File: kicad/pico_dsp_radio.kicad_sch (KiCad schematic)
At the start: 26 parts, among them J1 Conn_01x02, J2 MJ-8435, J3 Conn_01x12, Q1 IRLML6402, SW1 SW_SPDT, U1 Pico, U2 MCP73831-2-OT, U3 KT0913, Y1 32.768K12.5PI/4115E

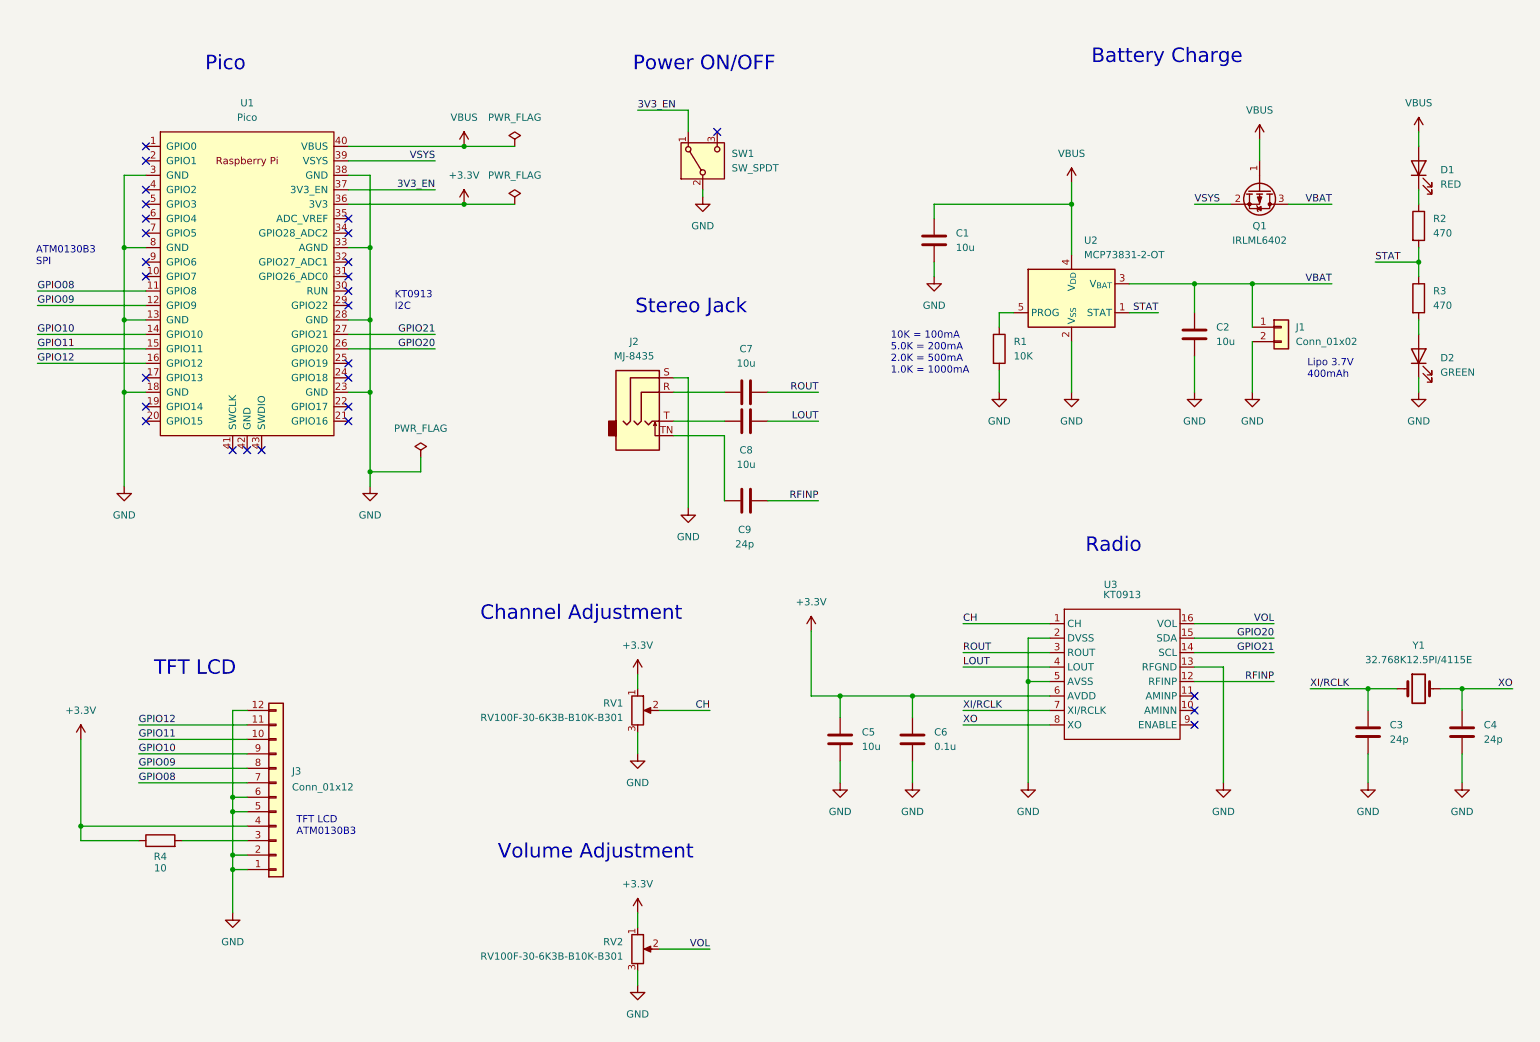
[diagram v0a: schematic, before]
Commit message: feat: Change switch to a slide switch
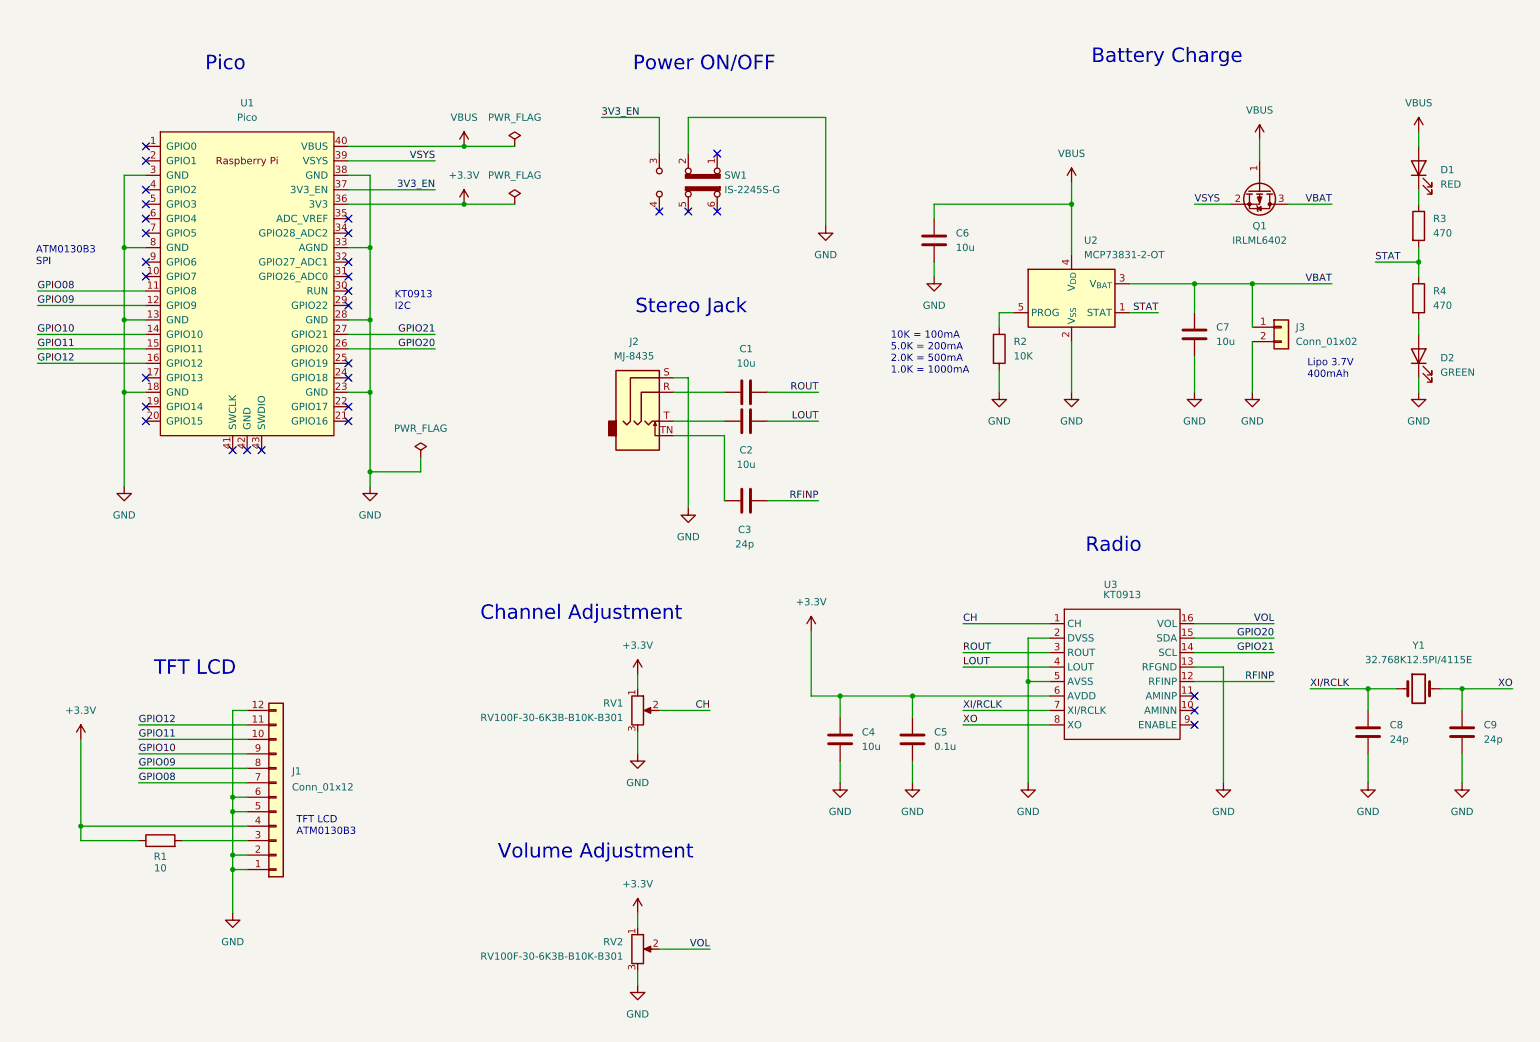
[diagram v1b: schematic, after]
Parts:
- removed SW1: SW_SPDT, symbol Switch:SW_SPDT
- added SW1: IS-2245S-G, symbol Switch:SW_Slide_DPDT
- renumbered C7 to C1, C8 to C2, C9 to C3, C5 to C4, C6 to C5, C1 to C6, C2 to C7, C3 to C8, C4 to C9, J3 to J1, J1 to J3, R4 to R1, R1 to R2, R2 to R3, R3 to R4
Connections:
- net 3V3_EN: now also SW1.3 (C)
- net GND: now also SW1.2 (B)
- no-connect marks 28 -> 31

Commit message: feat: Added a switch for toggling between the speaker and earphones
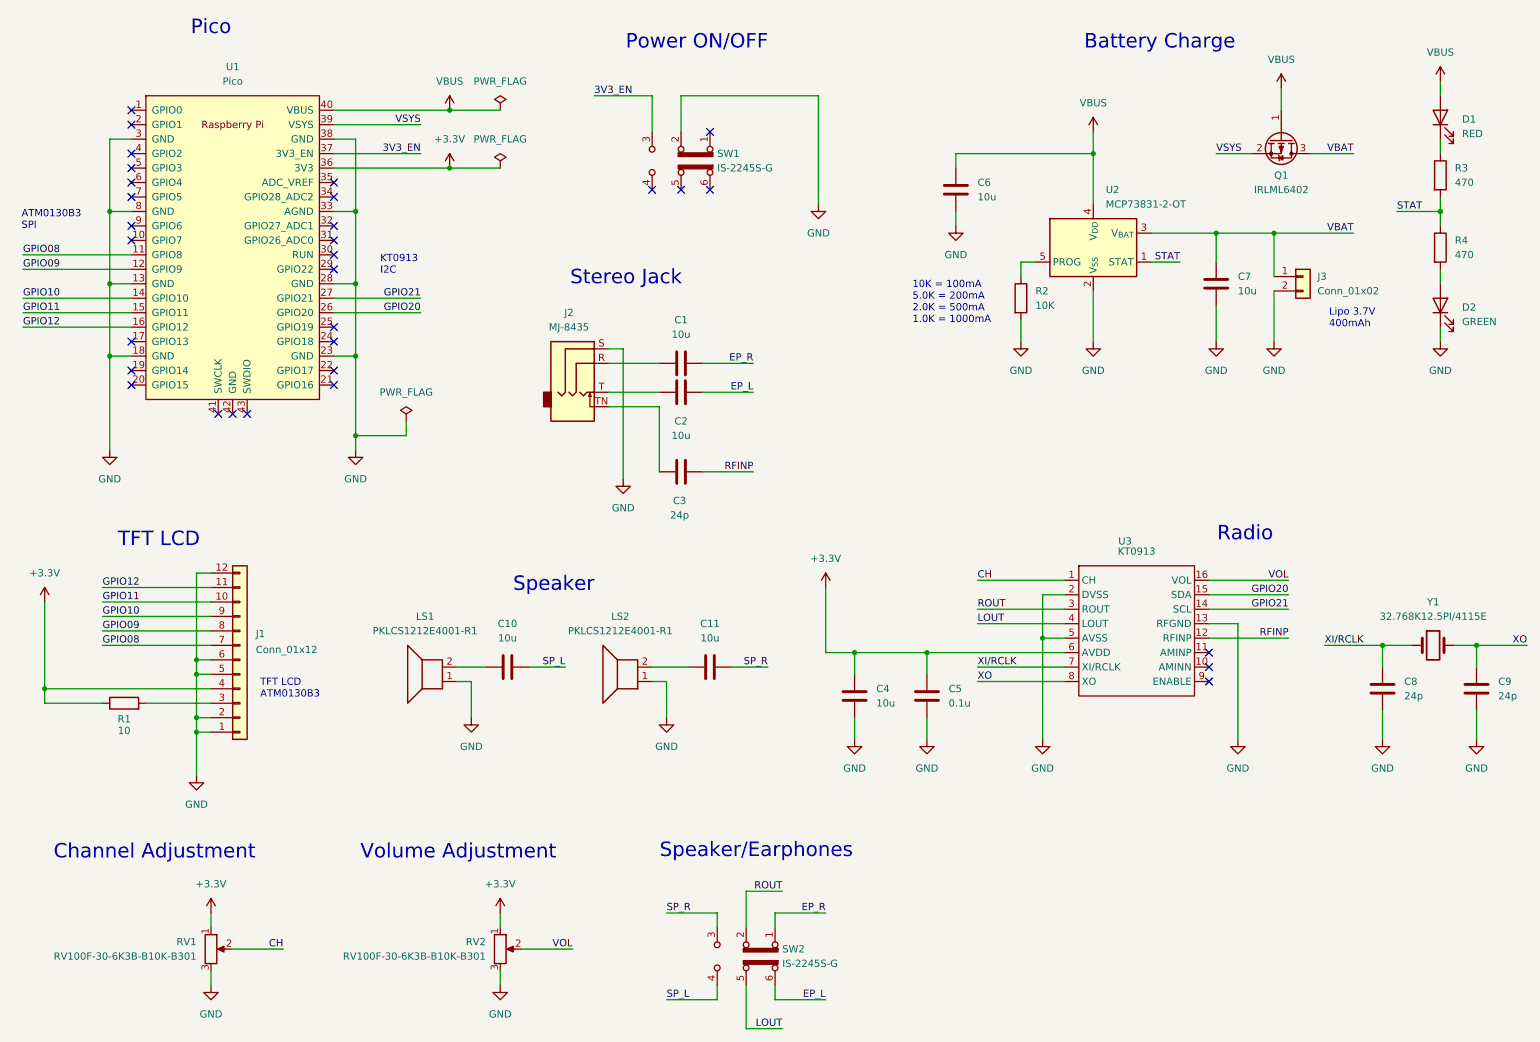
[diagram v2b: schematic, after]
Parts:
- added C10, C11: 10u, symbol Device:C
- added LS1, LS2: PKLCS1212E4001-R1, symbol Device:Speaker
- added SW2: IS-2245S-G, symbol Switch:SW_Slide_DPDT
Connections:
- net GND: now also LS1.1, LS2.1
- net LOUT: now also SW2.5 (B); no longer C2.1
- net ROUT: now also SW2.2 (B); no longer C1.2
- new net: C10.1, LS1.2
- new net: C11.1, LS2.2
- new net EP_L: C2.1, SW2.6 (C)
- new net EP_R: C1.2, SW2.1 (A)
- new net SP_L: C10.2, SW2.4 (A)
- new net SP_R: C11.2, SW2.3 (C)
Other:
- note added: "Speaker"
- note added: "Speaker/Earphones"
- moved on the sheet: C1, C2, C3, C4, C5, C6, C7, C8, C9, D1, D2, J1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

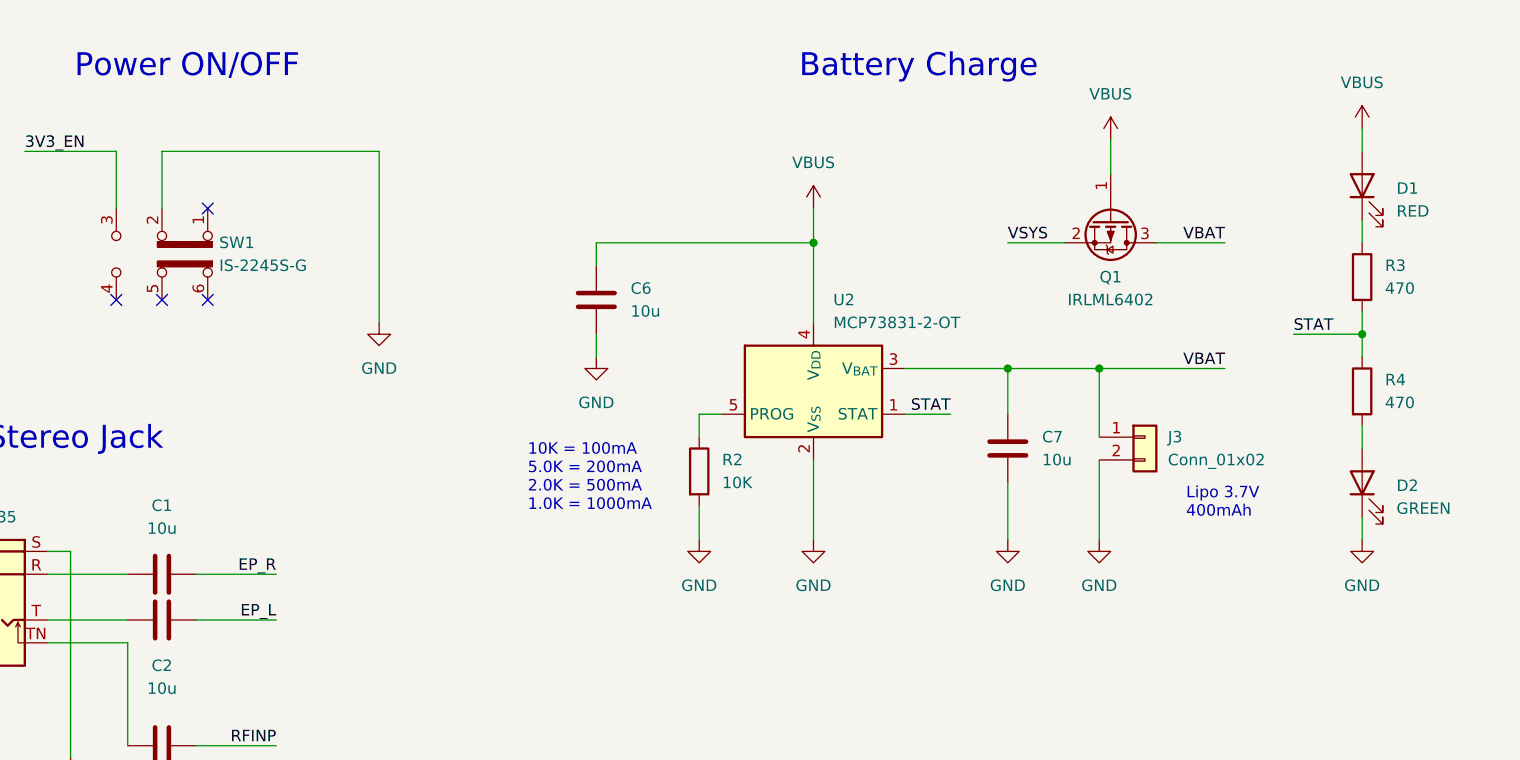
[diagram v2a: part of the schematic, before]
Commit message: feat: Added the model number for the LED
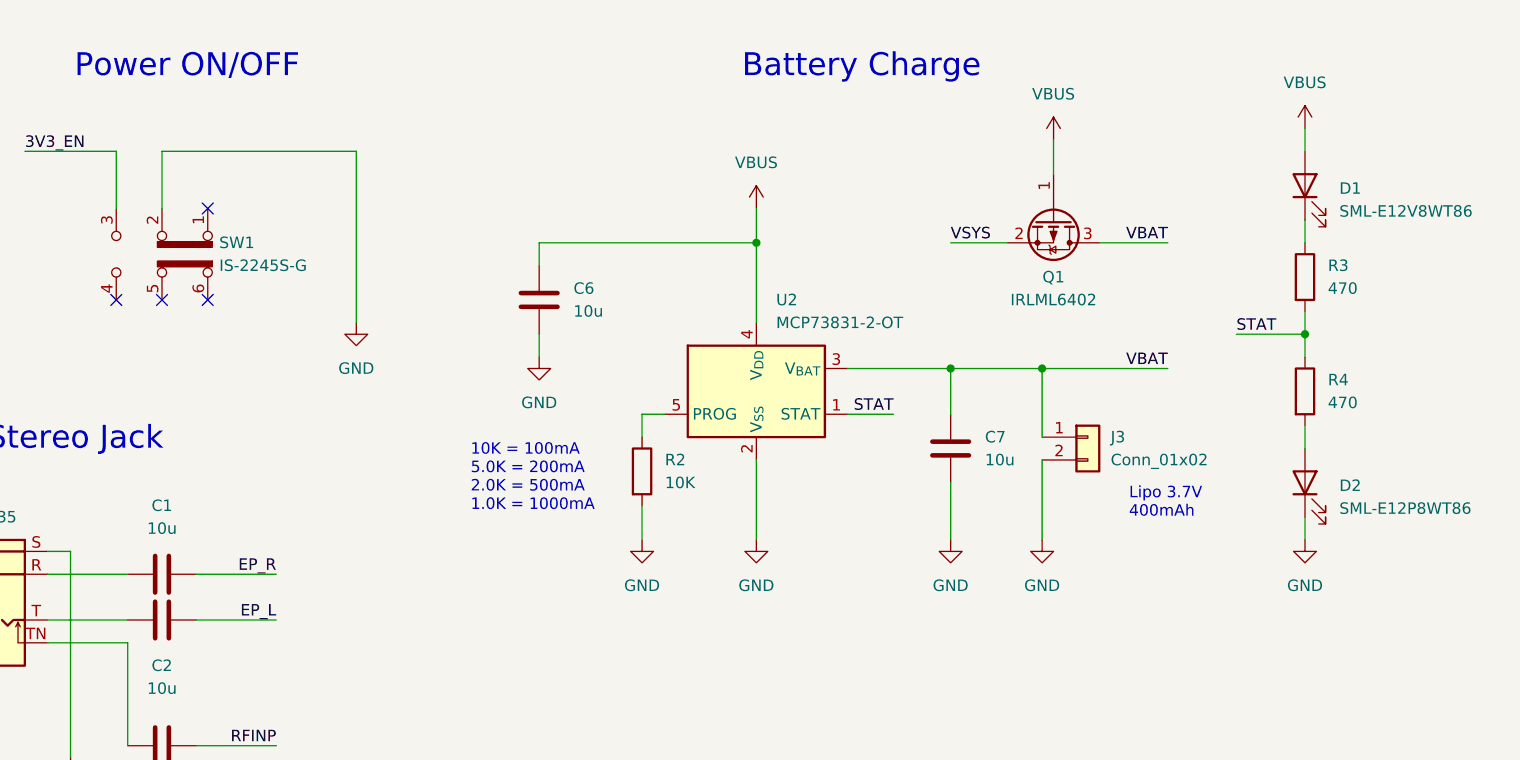
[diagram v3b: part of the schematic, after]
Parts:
- D1: value RED -> SML-E12V8WT86
- D2: value GREEN -> SML-E12P8WT86
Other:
- moved on the sheet: C6, C7, D1, D2, J3, Q1, R2, R3, R4, U2
